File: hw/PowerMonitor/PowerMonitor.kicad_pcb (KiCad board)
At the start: 4 copper layers, 100 x 100 mm, 157 parts, among them J1 Conn_01x02_Socket, J2 Conn_01x02_Socket, J3 Conn_01x02_Socket, J4 Conn_01x02_Socket, J5 Conn_01x02_Socket, K1 Relay_SPST-NO, Q1 AO3400A, Q10 AO3400A, Q11 AO3400A, Q12 AO3400A, Q13 AO3400A, Q14 X0202MN, Q15 Q_PMOS_GDS, Q16 AO3400A, Q17 AO3400A, Q18 AO3400A, Q19 Q_PMOS_GDS, Q2 AO3400A, Q20 AO3400A, Q3 Q_PMOS_GDS, Q4 AO3400A, Q5 AO3400A, Q6 AO3400A, Q7 AO3400A, Q8 AO3400A, Q9 AO3400A, SW1 SW_Wuerth_450301014042, U1 LM393, U2 LM358, U3 LM393, U4 INA129, U5 LM358, U6 LM393, U7 LM393, U8 LM358

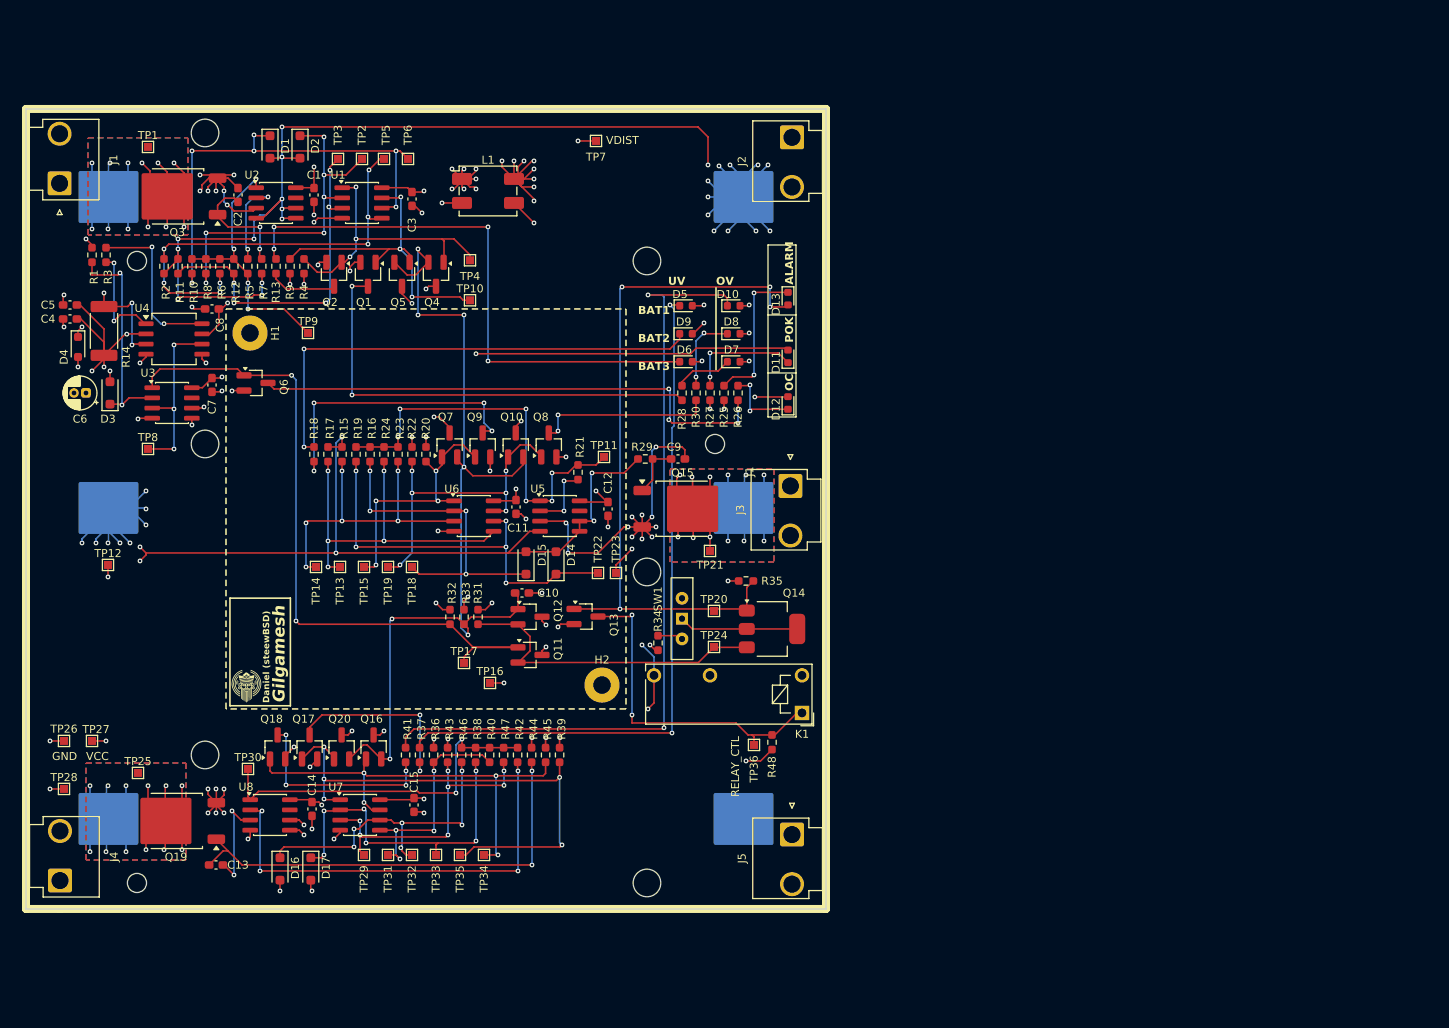
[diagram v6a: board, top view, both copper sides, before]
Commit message: powmon: add more vias for power signals
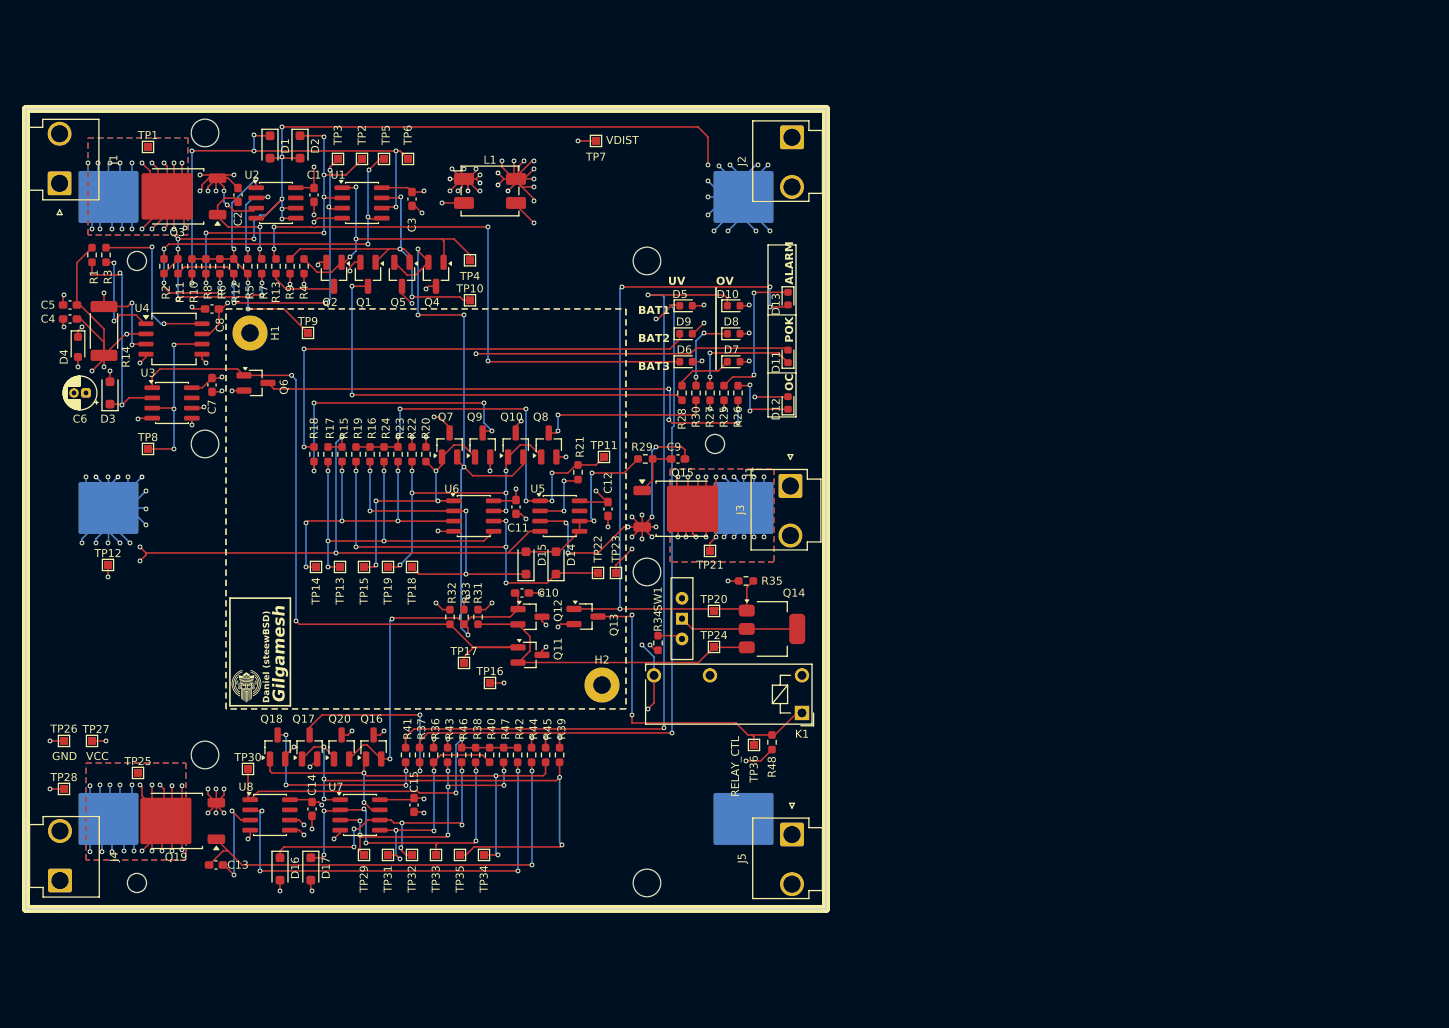
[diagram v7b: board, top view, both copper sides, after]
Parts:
- moved L1 0.25 mm to (153.8, 50.8)
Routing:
- net /CellMonitor1/VbatH: track 56.3 -> 102.1 mm, vias 12 -> 20
- net /CellMonitor3/VbatH: track 57.9 -> 97.3 mm, vias 12 -> 20
- net /CellMonitor2/VbatH: track 62.8 -> 96.0 mm, vias 12 -> 20
- net /CellMonitor1/Vprot: track 160.3 -> 188.8 mm, vias 23 -> 29
- net +10V: track 111.8 -> 118.7 mm, vias 33 -> 32
- net VDC: track 54.0 -> 59.7 mm, vias 9 -> 12
- net /VDIST: track 25.8 -> 30.3 mm, vias 9 -> 12
- net Net-(D5-K): track 87.8 -> 90.3 mm

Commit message: powmon: change plane connections to solid and add vias
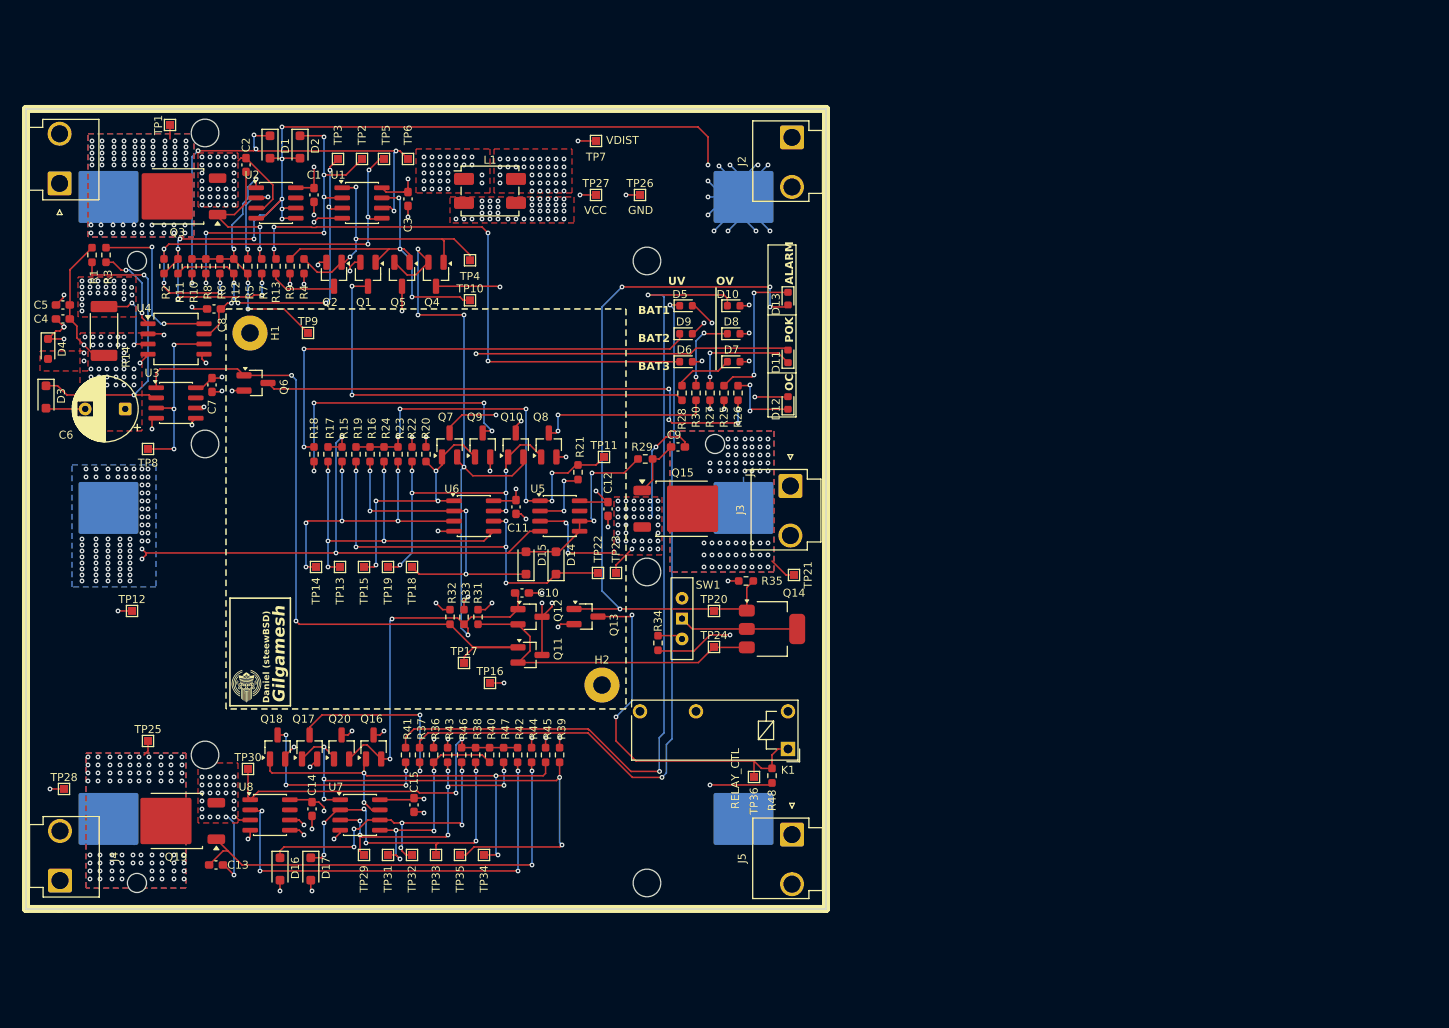
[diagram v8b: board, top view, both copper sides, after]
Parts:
- C6: footprint Capacitor_THT:CP_Radial_D4.0mm_P1.50mm -> Capacitor_THT:CP_Radial_D8.0mm_P5.00mm
- R1: value 150 -> 150R
- R25: value 100 -> 100R
- moved TP26 99.2 mm to (172.5, 51.2)
- moved TP27 92.9 mm to (167.0, 51.2)
- moved TP21 10.9 mm to (191.8, 98.8), turned to -90 degrees
- moved D3 8.02 mm to (98.2, 76.5), turned to -90 degrees
- moved TP12 6.49 mm to (109.0, 103.2)
- moved C6 5.29 mm to (108.2, 78.0)
- moved K1 4.83 mm to (191.0, 120.5)
- moved TP25 4.19 mm to (111.0, 119.5)
- moved R48 4.18 mm to (189.0, 123.8)
- moved TP36 4.00 mm to (186.8, 124.0)
- moved TP1 3.89 mm to (113.8, 42.5), turned to 90 degrees
- moved C2 3.88 mm to (123.2, 47.5)
- moved D4 3.76 mm to (98.5, 70.5)
- moved C9 1.50 mm to (177.2, 82.8)
- moved C4 0.89 mm to (100.4, 66.8)
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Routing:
- net /CellMonitor1/VbatH: track 102.1 -> 21.3 mm, vias 20 -> 76
- net /CellMonitor2/VbatH: track 96.0 -> 33.4 mm, vias 20 -> 61
- net /CellMonitor1/Vprot: track 188.8 -> 132.3 mm, vias 29 -> 104
- net /CellMonitor3/VbatH: track 97.3 -> 44.1 mm, vias 20 -> 70
- net /VDIST: track 30.3 -> 2.25 mm, vias 12 -> 36
- net VDC: track 59.7 -> 41.1 mm, vias 12 -> 30
- net /CellMonitor2/Vprot: track 225.3 -> 208.8 mm, vias 35 -> 60
- net /CellMonitor3/Vprot: track 35.3 -> 21.3 mm, vias 10 -> 55
- net Net-(D3-K): track 27.5 -> 38.4 mm
- net +10V: track 118.7 -> 127.0 mm, vias 32 -> 61
- net Net-(D10-K): track 101.1 -> 108.4 mm
- net Net-(Q13-D): track 42.2 -> 47.8 mm
- net Net-(D5-K): track 90.3 -> 94.7 mm
- net Net-(Q3-G): track 14.5 -> 18.2 mm
- net Net-(D13-A): track 89.4 -> 91.3 mm
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- added copper zone on F.Cu, net +10V
- added copper zone on B.Cu, net /CellMonitor1/Vprot
- added copper zone on F.Cu, net /CellMonitor1/Vprot
- added copper zone on F.Cu, net /CellMonitor2/Vprot
- added copper zone on F.Cu, net /CellMonitor3/Vprot
- added copper zone on F.Cu, net /VDIST
- added copper zone on F.Cu, net GND
- added copper zone on F.Cu, net VDC
